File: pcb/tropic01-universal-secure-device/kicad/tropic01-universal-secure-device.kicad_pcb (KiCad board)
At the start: 4 copper layers, 42.7 x 36 mm, 96 parts, among them J1 USB4105-GF-A, J2 ER-TFT024IPS-3 50P FFC, J6 SM04B-SRSS-TB, J7 SWD_TC2030, J9 S2B-PH-SM4-TB, SW1 EVQP7J01P, U1 STM32U585VIT6, U10 BQ24074RGTR, U11 OPTIGA-TRUST-M-SLS32AIA, U13 TPS22917DBVR, U14 TPS22917DBVR, U15 TPS61165DBVR, U2 TR01-C2P-T301, U3 TPS62840DLCR, U4 TPS22917DBVR, U5 W25Q128JVSIQ, U7 TPD4E05U06DQAR, U8 TPS2553DBVR, U9 ST25R3916B-AQET, X1 16MHz, X3 FA-238 27.12MHz

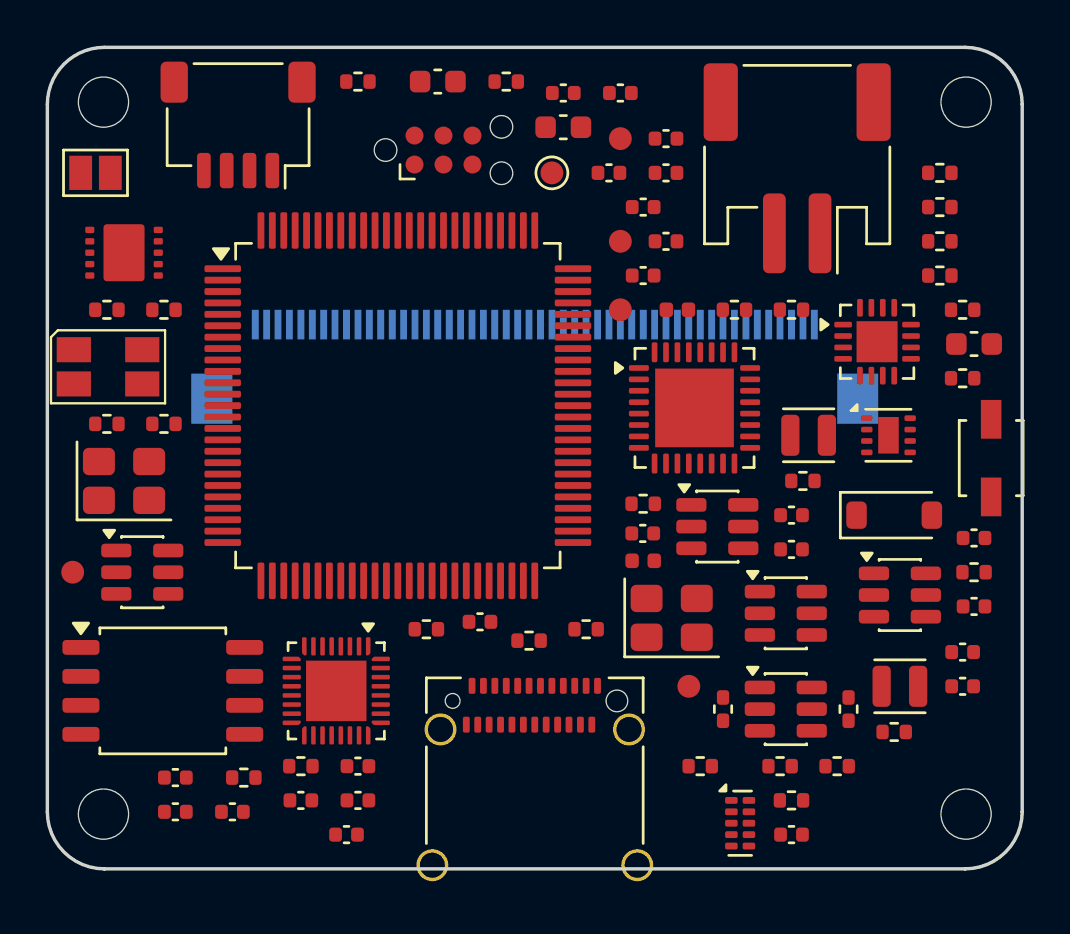
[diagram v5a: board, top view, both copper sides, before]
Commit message: improve(pcb): adjacency-priority passive placement
Re-place passives with adjacency-critical ordering (crystals first, then
CT caps, decoupling, then bulk last) so the parts that NEED to be close
are close on this capacity-limited board:
- HSE crystal load caps C18/C19 now 2.5/3.2mm from X1 (was ~16mm).
- NFC crystal caps C34/C35 2.9mm from X3; CT caps C7/C8 2.8/3.5mm.
- TROPIC SPI stays 2.9mm. DRC clean.
Accepted density compromises (board is full, zero-sum): C6 TROPIC CT cap
9.6mm, R7 I2C pull-up far (SE2_I2C_SDA 16.8mm), RGB LED resistors far
(length irrelevant). Audit: all constraints met; all parts useful; the
7 NFC matching parts (ANT1+C30-33+L30-31) are intentional tuning-gated
placeholders (unconnected until first-article RF measurement).
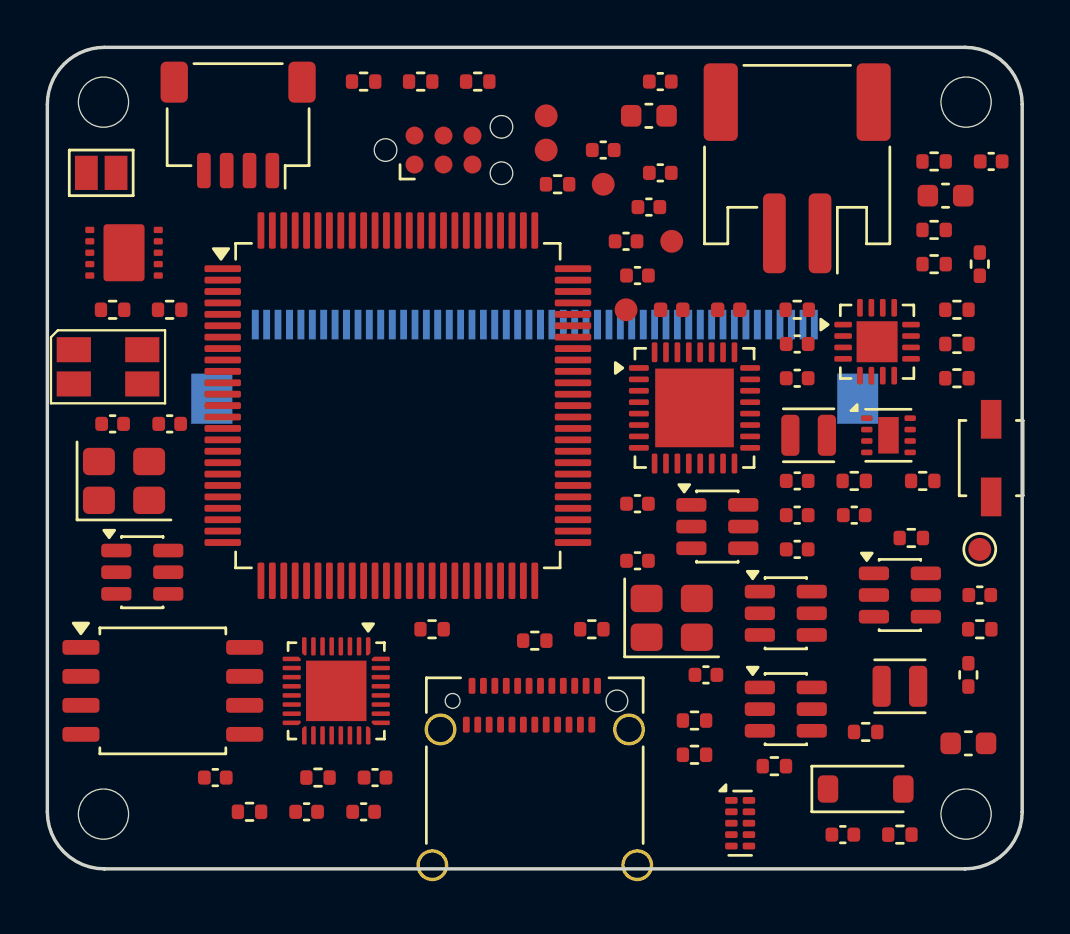
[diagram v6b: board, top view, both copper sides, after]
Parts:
- moved C17 37.2 mm to (37.5, 35.5)
- moved TP_GND 30.0 mm to (38.0, 42.5)
- moved C16 29.3 mm to (45.5, 68.5)
- moved R23 27.3 mm to (49.5, 39.0)
- moved TP_UART_GND 25.0 mm to (51.5, 56.0)
- moved RLED1 24.1 mm to (29.5, 35.5)
- moved R24 23.2 mm to (48.0, 68.5)
- moved C1 22.8 mm to (50.0, 40.5)
- moved RLED2 22.4 mm to (33.0, 40.0)
- moved C32 21.5 mm to (43.5, 47.0)
- moved R20 20.3 mm to (51.5, 43.5)
- moved C33 18.7 mm to (43.5, 53.0)
- moved C18 18.4 mm to (13.5, 50.5)
- moved C31 18.3 mm to (36.5, 54.0)
- moved C15 17.5 mm to (51.0, 64.5)
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
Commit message: fix(pcb): USB-C posts on-board (extend bottom +0.8mm) + clean silk -> DRC 0
Severe review fixes:
- USB-C J1: its 4 PTH shield/mounting posts are normal, but the 2 FRONT
  posts were breaking the bottom board edge (hole/pad past y=70) because
  an 11.7mm-deep USB-C must overhang a 36mm board. Moving it up doesn't
  fit (NFC crystal X3 then has no home - board is full). Fix: extend the
  bottom edge +0.8mm (height 36->36.8; width unchanged=hard constraint;
  still within display+battery envelope 59.26mm). Front-post pad-bottom
  now 70.54 < edge 70.8. Bottom corner holes MH1/MH2 moved down to stay
  seated in the new fillets.
- Moved SW1 (side-button) silk outline to F.Fab (was crossing the edge).
- Result: DRC = 0 violations (was 5 accepted exceptions).
Audit confirmed: all constraints met, all parts useful, silk text hidden.
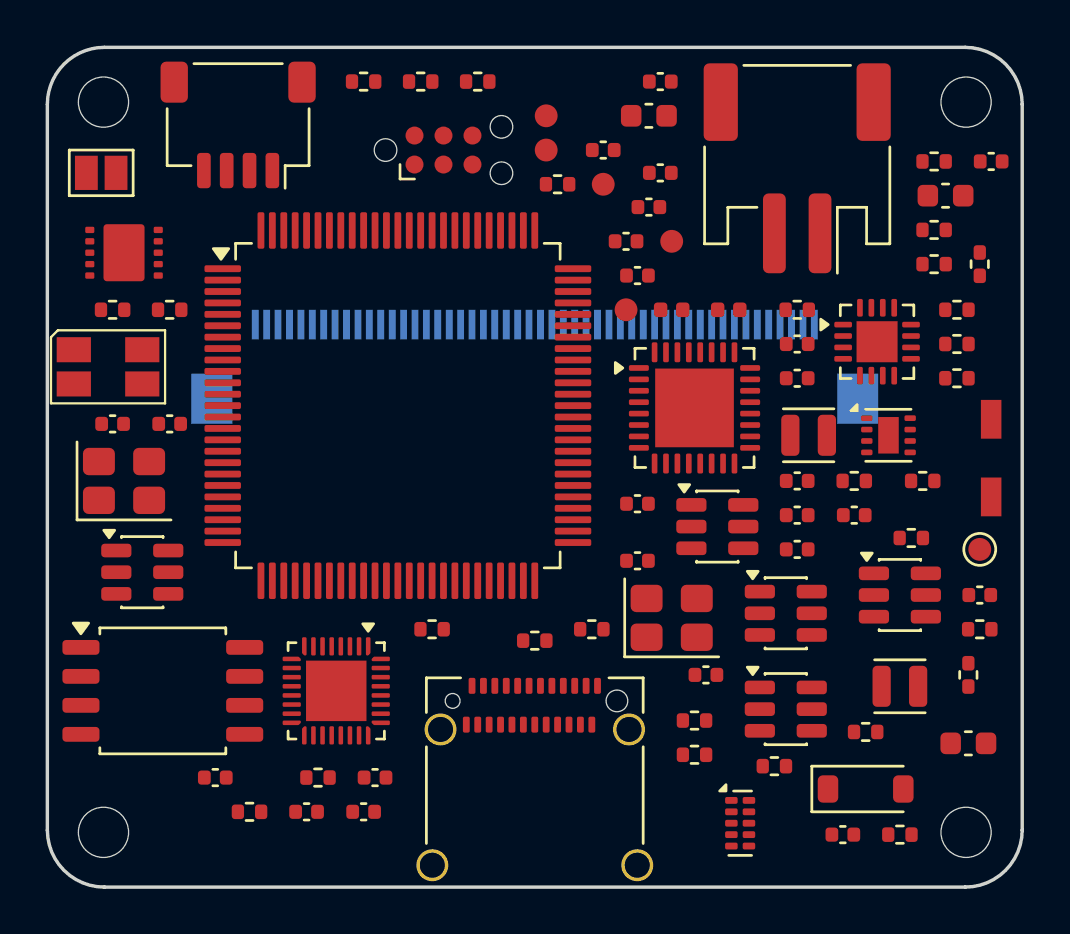
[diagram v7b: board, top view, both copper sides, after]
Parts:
- moved MH1 0.80 mm to (13.1, 68.4)
- moved MH2 0.80 mm to (50.9, 68.4)
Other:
- board size 42.7 x 36 mm -> 42.7 x 36.8 mm
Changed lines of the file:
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@@
 		(duplicate_pad_numbers_are_jumpers no)
 		(fp_line
-			(start 1.65 -1.4)
-			(end 1.65 -1.1)
+			(start 2.4 -1.65)
+			(end -2.4 -1.65)
 			(stroke
-				(width 0.12)
+				(width 0.05)
 				(type solid)
 			)
-			(layer "F.SilkS")
+			(layer "F.CrtYd")
 		)
 		(fp_line
-			(start -1.65 -1.4)
-			(end 1.65 -1.4)
+			(start -2.4 -1.65)
+			(end -2.4 1.65)
 			(stroke
-				(width 0.12)
+				(width 0.05)
 				(type solid)
 			)
-			(layer "F.SilkS")
+			(layer "F.CrtYd")
 		)
 		(fp_line
-			(start -1.65 -1.1)
-			(end -1.65 -1.4)
+			(start 2.4 1.65)
+			(end 2.4 -1.65)
 			(stroke
-				(width 0.12)
+				(width 0.05)
 				(type solid)
 			)
-			(layer "F.SilkS")
+			(layer "F.CrtYd")
 		)
 		(fp_line
-			(start -1.65 1.1)
-			(end -1.65 1.4)
+			(start -2.4 1.65)
+			(end 2.4 1.65)
 			(stroke
-				(width 0.12)
+				(width 0.05)
 				(type solid)
 			)
-			(layer "F.SilkS")
+			(layer "F.CrtYd")
 		)
 		(fp_line
-			(start 1.65 1.4)
-			(end 1.65 1.1)
+			(start 1.65 -1.4)
+			(end 1.65 -1.1)
 			(stroke
 				(width 0.12)
 				(type solid)
 			)
-			(layer "F.SilkS")
+			(layer "F.Fab")
 		)
 		(fp_line
-			(start -1.65 1.4)
-			(end 1.65 1.4)
+			(start -1.65 -1.4)
+			(end 1.65 -1.4)
 			(stroke
 				(width 0.12)
 				(type solid)
 			)
-			(layer "F.SilkS")
+			(layer "F.Fab")
 		)
 		(fp_line
-			(start 2.4 -1.65)
-			(end -2.4 -1.65)
+			(start 1.5 -1.25)
+			(end 1.5 1.25)
 			(stroke
-				(width 0.05)
+				(width 0.1)
 				(type solid)
 			)
-			(layer "F.CrtYd")
+			(layer "F.Fab")
 		)
 		(fp_line
-			(start -2.4 -1.65)
-			(end -2.4 1.65)
+			(start -1.5 -1.25)
+			(end 1.5 -1.25)
 			(stroke
-				(width 0.05)
+				(width 0.1)
 				(type solid)
 			)
-			(layer "F.CrtYd")
+			(layer "F.Fab")
 		)
 		(fp_line
-			(start 2.4 1.65)
-			(end 2.4 -1.65)
+			(start -1.65 -1.1)
+			(end -1.65 -1.4)
 			(stroke
-				(width 0.05)
+				(width 0.12)
 				(type solid)
 			)
-			(layer "F.CrtYd")
+			(layer "F.Fab")
 		)
 		(fp_line
-			(start -2.4 1.65)
-			(end 2.4 1.65)
+			(start -1.65 1.1)
+			(end -1.65 1.4)
 			(stroke
-				(width 0.05)
+				(width 0.12)
 				(type solid)
 			)
-			(layer "F.CrtYd")
+			(layer "F.Fab")
 		)
 		(fp_line
-			(start 1.5 -1.25)
-			(end 1.5 1.25)
+			(start 1.5 1.25)
+			(end -1.5 1.25)
 			(stroke
 				(width 0.1)
@@
 		)
 		(fp_line
-			(start -1.5 -1.25)
-			(end 1.5 -1.25)
+			(start -1.5 1.25)
+			(end -1.5 -1.25)
 			(stroke
 				(width 0.1)
@@
 		)
 		(fp_line
-			(start 1.5 1.25)
-			(end -1.5 1.25)
+			(start 1.65 1.4)
+			(end 1.65 1.1)
 			(stroke
-				(width 0.1)
+				(width 0.12)
 				(type solid)
 			)
@@
 		)
 		(fp_line
-			(start -1.5 1.25)
-			(end -1.5 -1.25)
+			(start -1.65 1.4)
+			(end 1.65 1.4)
 			(stroke
-				(width 0.1)
+				(width 0.12)
 				(type solid)
 			)
@@
 	(footprint "nSealr_Mechanical:MountingHole_M2_Clearance_NPTH"
 		(layer "F.Cu")
-		(at 13.1 67.6)
+		(at 13.1 68.4)
 		(descr "Compact M2 clearance NPTH case screw/standoff hole; can also receive a locating pin")
 		(property "Reference" "MH1"
@@
 	(footprint "nSealr_Mechanical:MountingHole_M2_Clearance_NPTH"
 		(layer "F.Cu")
-		(at 50.9 67.6)
+		(at 50.9 68.4)
 		(descr "Compact M2 clearance NPTH case screw/standoff hole; can also receive a locating pin")
 		(property "Reference" "MH2"
@@
 	)
 	(gr_line
-		(start 10.64 67.5)
+		(start 10.64 68.3)
 		(end 10.64 36.5)
 		(stroke
@@
 	)
 	(gr_arc
-		(start 13.14 70)
-		(mid 11.372233 69.267766)
-		(end 10.64 67.5)
+		(start 13.14 70.8)
+		(mid 11.372233 70.067766)
+		(end 10.64 68.3)
 		(stroke
 			(width 0.15)
@@
 	)
 	(gr_line
-		(start 50.86 70)
-		(end 13.14 70)
+		(start 50.86 70.8)
+		(end 13.14 70.8)
 		(stroke
 			(width 0.15)
@@
 	(gr_line
 		(start 53.36 36.5)
-		(end 53.36 67.5)
+		(end 53.36 68.3)
 		(stroke
 			(width 0.15)
@@
 	)
 	(gr_arc
-		(start 53.36 67.5)
-		(mid 52.627766 69.267766)
-		(end 50.86 70)
+		(start 53.36 68.3)
+		(mid 52.627766 70.067766)
+		(end 50.86 70.8)
 		(stroke
 			(width 0.15)

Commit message: improve(pcb): group UART test points + nudge RGB LED off the edge
Review follow-ups from visual inspection:
- TP_UART_GND was at (51.5,56), ~20mm from TP_UART_RX/TX. Grouped all
  three into a tight L-cluster (1.6mm) so the serial console (TX/RX/GND)
  is probeable together; kept off the NFC antenna keep-out (ANT1 spans
  x21.3-42.7, y33.8-38.2).
- RGB LED1 copper was 0.41mm from the left board edge; nudged inward to
  0.91mm clearance (still left-edge, top-emitting).
DRC = 0. Note: board is PLACED, not yet ROUTED (0 tracks).
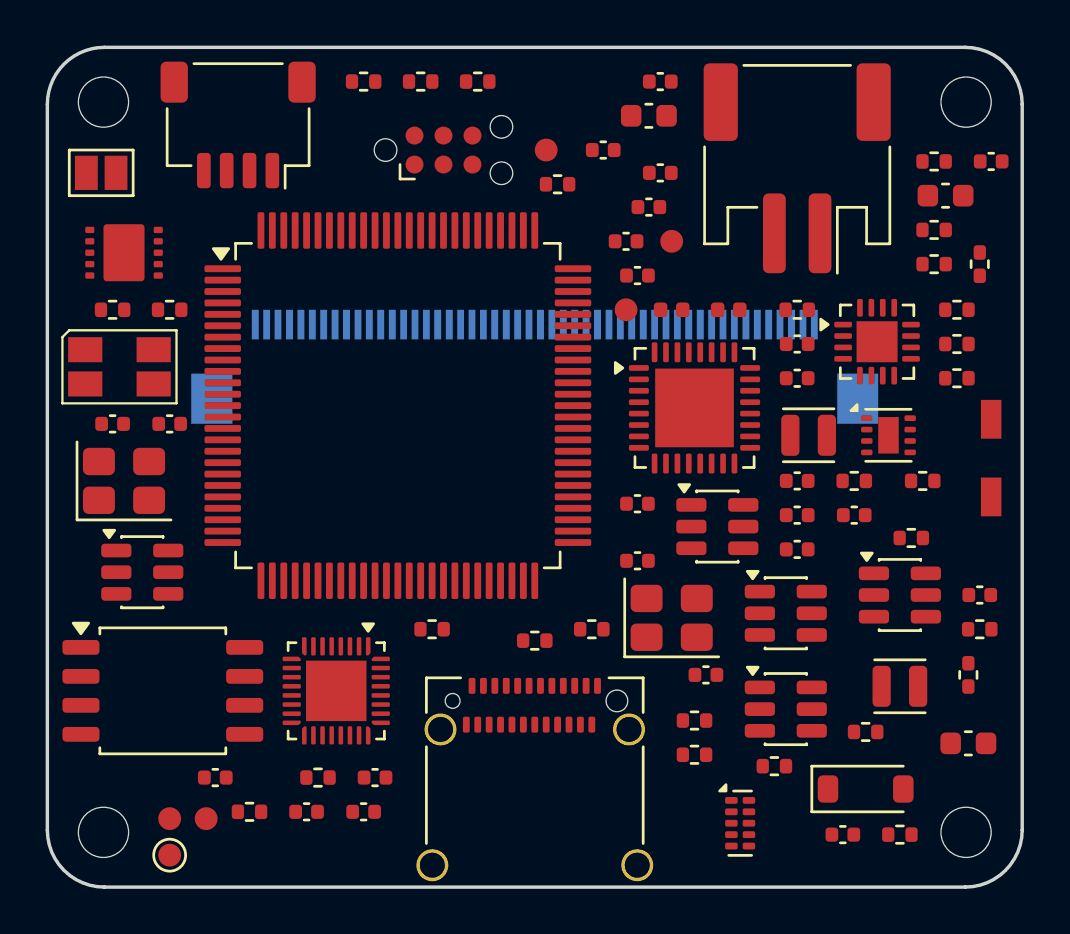
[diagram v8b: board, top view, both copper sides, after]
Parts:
- moved TP_UART_GND 37.9 mm to (16.0, 69.4)
- moved TP_UART_RX 34.2 mm to (17.6, 67.8)
- moved TP_UART_TX 33.7 mm to (16.0, 67.8)
- moved LED1 0.50 mm to (13.8, 48.0)
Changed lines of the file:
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@@
 	(footprint "TestPoint:TestPoint_Pad_D1.0mm"
 		(layer "F.Cu")
-		(at 35 40)
+		(at 16 67.8)
 		(descr "Hidden back-side pogo/test pad")
 		(property "Reference" "TP_UART_TX"
@@
 	(footprint "TestPoint_Pad_D1.0mm"
 		(layer "F.Cu")
-		(at 51.5 56)
+		(at 16 69.399999)
 		(descr "SMD pad as test Point, diameter 1.0mm")
 		(tags "test point SMD pad")
@@
 	(footprint "LED_Avago_PLCC4_3.2x2.8mm_CW"
 		(layer "F.Cu")
-		(at 13.3 48)
+		(at 13.8 48)
 		(descr "3.2mm x 2.8mm PLCC4 RGB LED, https://docs.broadcom.com/docs/AV02-4186EN")
 		(tags "LED Avago PLCC-4 3528 ASMB-MTB0-0A3A2")
@@
 	(footprint "TestPoint:TestPoint_Pad_D1.0mm"
 		(layer "F.Cu")
-		(at 32.5 37)
+		(at 17.6 67.8)
 		(descr "Hidden back-side pogo/test pad")
 		(property "Reference" "TP_UART_RX"
